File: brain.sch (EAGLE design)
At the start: 24 parts, among them IC1 LP2950ACZ-3.3, IC2 LP2950ACZ-3.3, U1 TINY45-20-DIP, U4 TINY45-20-DIP, U5 TINY45-20-DIP, U6 TINY45-20-DIP

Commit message: Added routing. Looks like everything should be good. Put in via line because the $33 boards don't support scoring.
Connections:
- removed net N$14: U5.PB3(ADC3)
- removed net N$7: U4.PB2(SCK/ADC1)
- new net PB22: U4.PB2(SCK/ADC1), U5.PB2(SCK/ADC1)
- net TX2: now also U5.PB3(ADC3); no longer U5.PB2(SCK/ADC1)
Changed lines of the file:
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@@
 </segment>
 <segment>
-<pinref part="U5" gate="G$1" pin="PB2(SCK/ADC1)"/>
-<wire x1="99.06" y1="-187.96" x2="101.6" y2="-187.96" width="0.1524" layer="91"/>
+<pinref part="U5" gate="G$1" pin="PB3(ADC3)"/>
+<wire x1="99.06" y1="-190.5" x2="101.6" y2="-190.5" width="0.1524" layer="91"/>
+<label x="101.6" y="-190.5" size="1.778" layer="95"/>
 </segment>
 </net>
@@
 <pinref part="U5" gate="G$1" pin="PB4(ADC2)"/>
 <wire x1="99.06" y1="-193.04" x2="101.6" y2="-193.04" width="0.1524" layer="91"/>
+<label x="101.6" y="-193.04" size="1.778" layer="95"/>
 </segment>
 </net>
 <net name="PB12" class="0">
+<segment>
+<pinref part="U5" gate="G$1" pin="PB1(MISO)"/>
+<wire x1="99.06" y1="-185.42" x2="101.6" y2="-185.42" width="0.1524" layer="91"/>
+<label x="101.6" y="-185.42" size="1.778" layer="95"/>
+</segment>
 <segment>
 <pinref part="U4" gate="G$1" pin="PB1(MISO)"/>
@@
 <pinref part="LED1" gate="G$1" pin="A"/>
 <wire x1="149.86" y1="-152.4" x2="157.48" y2="-152.4" width="0.1524" layer="91"/>
-</segment>
-<segment>
-<pinref part="U5" gate="G$1" pin="PB1(MISO)"/>
-<wire x1="99.06" y1="-185.42" x2="101.6" y2="-185.42" width="0.1524" layer="91"/>
+<label x="101.6" y="-154.94" size="1.778" layer="95"/>
 </segment>
 </net>
@@
 <pinref part="U4" gate="G$1" pin="PB0(MOSI)"/>
 <wire x1="99.06" y1="-152.4" x2="101.6" y2="-152.4" width="0.1524" layer="91"/>
+<label x="101.6" y="-152.4" size="1.778" layer="95"/>
 </segment>
 <segment>
 <pinref part="U5" gate="G$1" pin="PB0(MOSI)"/>
 <wire x1="99.06" y1="-182.88" x2="101.6" y2="-182.88" width="0.1524" layer="91"/>
-</segment>
-</net>
-<net name="N$7" class="0">
-<segment>
-<pinref part="U4" gate="G$1" pin="PB2(SCK/ADC1)"/>
-<wire x1="99.06" y1="-157.48" x2="101.6" y2="-157.48" width="0.1524" layer="91"/>
-</segment>
-</net>
-<net name="N$14" class="0">
-<segment>
-<pinref part="U5" gate="G$1" pin="PB3(ADC3)"/>
-<wire x1="99.06" y1="-190.5" x2="101.6" y2="-190.5" width="0.1524" layer="91"/>
+<label x="101.6" y="-182.88" size="1.778" layer="95"/>
 </segment>
 </net>
@@
 <pinref part="U5" gate="G$1" pin="PB5(NRES)"/>
 <wire x1="99.06" y1="-195.58" x2="101.6" y2="-195.58" width="0.1524" layer="91"/>
+<label x="101.6" y="-195.58" size="1.778" layer="95"/>
 </segment>
 <segment>
 <pinref part="U4" gate="G$1" pin="PB5(NRES)"/>
 <wire x1="99.06" y1="-165.1" x2="101.6" y2="-165.1" width="0.1524" layer="91"/>
+<label x="101.6" y="-165.1" size="1.778" layer="95"/>
 </segment>
 </net>
@@
 </segment>
 </net>
+<net name="PB22" class="0">
+<segment>
+<pinref part="U5" gate="G$1" pin="PB2(SCK/ADC1)"/>
+<wire x1="99.06" y1="-187.96" x2="101.6" y2="-187.96" width="0.1524" layer="91"/>
+<label x="101.6" y="-187.96" size="1.778" layer="95"/>
+</segment>
+<segment>
+<pinref part="U4" gate="G$1" pin="PB2(SCK/ADC1)"/>
+<wire x1="99.06" y1="-157.48" x2="101.6" y2="-157.48" width="0.1524" layer="91"/>
+<label x="101.6" y="-157.48" size="1.778" layer="95"/>
+</segment>
+</net>

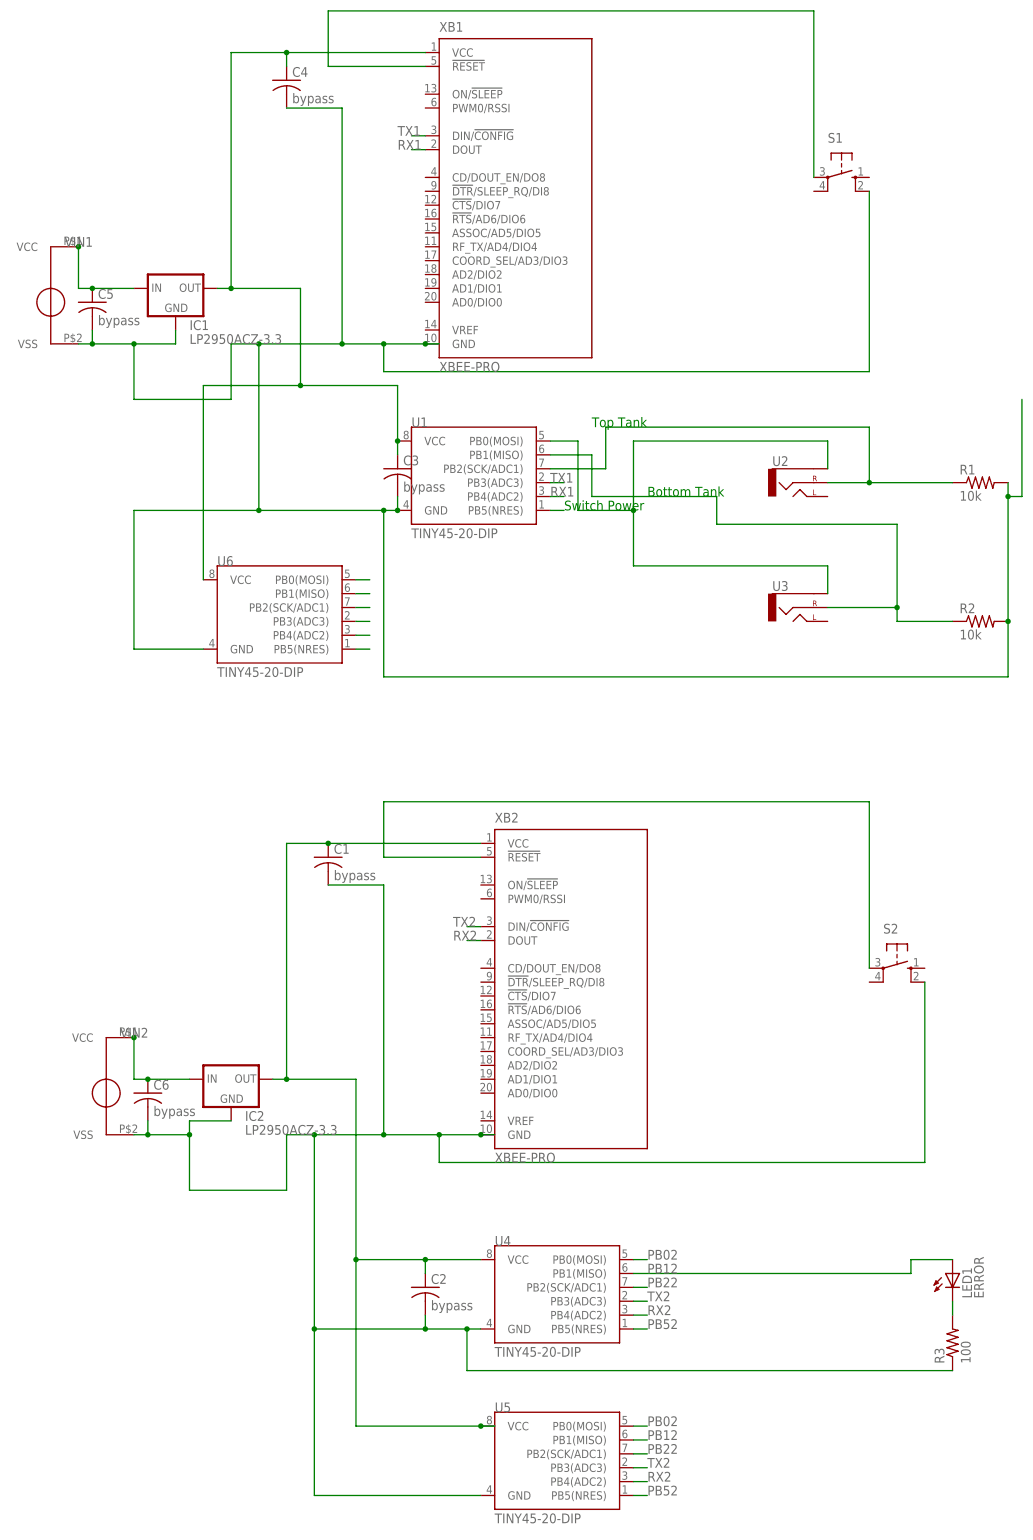
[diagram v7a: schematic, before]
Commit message: Added bypass capacitors per Sasha's request. Put some identifying information on bottom silkscreen.
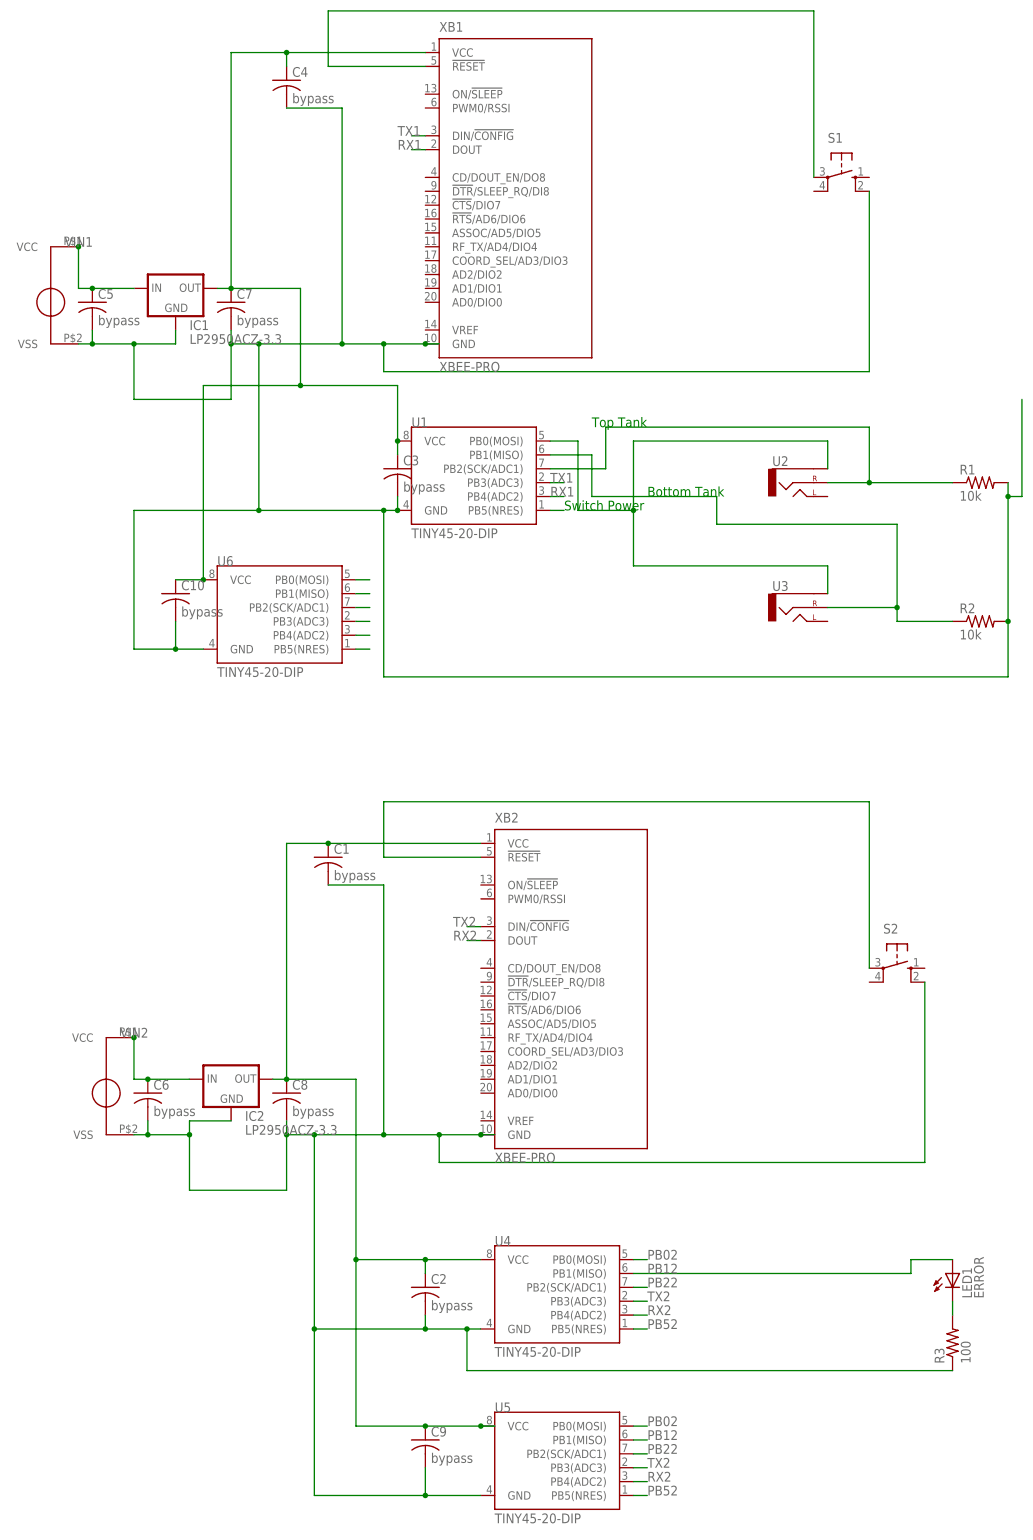
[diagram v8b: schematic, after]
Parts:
- added C10, C7, C8, C9: bypass, rcl:C-US050-025X075
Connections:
- net GND1: now also C10.2, C7.2
- net GND2: now also C8.2, C9.2
- net VCC1: now also C10.1, C7.1
- net VOUT2: now also C8.1, C9.1
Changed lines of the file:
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@@
 <part name="U5" library="SparkFun-DigitalIC" deviceset="ATTINY45" device="TINY45-20-DIP" value="TINY45-20-DIP"/>
 <part name="U6" library="SparkFun-DigitalIC" deviceset="ATTINY45" device="TINY45-20-DIP" value="TINY45-20-DIP"/>
+<part name="C7" library="rcl" deviceset="C-US" device="050-025X075" value="bypass"/>
+<part name="C8" library="rcl" deviceset="C-US" device="050-025X075" value="bypass"/>
+<part name="C9" library="rcl" deviceset="C-US" device="050-025X075" value="bypass"/>
+<part name="C10" library="rcl" deviceset="C-US" device="050-025X075" value="bypass"/>
 </parts>
 <sheets>
@@
 <instance part="U5" gate="G$1" x="86.36" y="-190.5"/>
 <instance part="U6" gate="G$1" x="35.56" y="-35.56"/>
+<instance part="C7" gate="G$1" x="25.4" y="22.86"/>
+<instance part="C8" gate="G$1" x="35.56" y="-121.92"/>
+<instance part="C9" gate="G$1" x="60.96" y="-185.42"/>
+<instance part="C10" gate="G$1" x="15.24" y="-30.48"/>
 </instances>
 <busses>
@@
 <wire x1="48.26" y1="-152.4" x2="48.26" y2="-182.88" width="0.1524" layer="91"/>
 <junction x="48.26" y="-152.4"/>
-<wire x1="48.26" y1="-182.88" x2="71.12" y2="-182.88" width="0.1524" layer="91"/>
+<wire x1="48.26" y1="-182.88" x2="60.96" y2="-182.88" width="0.1524" layer="91"/>
 <pinref part="U5" gate="G$1" pin="VCC"/>
+<wire x1="60.96" y1="-182.88" x2="71.12" y2="-182.88" width="0.1524" layer="91"/>
 <wire x1="73.66" y1="-182.88" x2="71.12" y2="-182.88" width="0.1524" layer="91"/>
 <junction x="71.12" y="-182.88"/>
+<pinref part="C8" gate="G$1" pin="1"/>
+<pinref part="C9" gate="G$1" pin="1"/>
+<junction x="60.96" y="-182.88"/>
 </segment>
 </net>
@@
 <junction x="40.64" y="-165.1"/>
 <pinref part="U5" gate="G$1" pin="GND"/>
-<wire x1="40.64" y1="-195.58" x2="71.12" y2="-195.58" width="0.1524" layer="91"/>
+<wire x1="40.64" y1="-195.58" x2="60.96" y2="-195.58" width="0.1524" layer="91"/>
+<pinref part="C8" gate="G$1" pin="2"/>
+<wire x1="60.96" y1="-195.58" x2="71.12" y2="-195.58" width="0.1524" layer="91"/>
+<wire x1="35.56" y1="-127" x2="35.56" y2="-129.54" width="0.1524" layer="91"/>
+<junction x="35.56" y="-129.54"/>
+<pinref part="C9" gate="G$1" pin="2"/>
+<wire x1="60.96" y1="-190.5" x2="60.96" y2="-195.58" width="0.1524" layer="91"/>
+<junction x="60.96" y="-195.58"/>
 </segment>
 </net>
@@
 <wire x1="7.62" y1="-15.24" x2="7.62" y2="-40.64" width="0.1524" layer="91"/>
 <pinref part="U6" gate="G$1" pin="GND"/>
-<wire x1="7.62" y1="-40.64" x2="20.32" y2="-40.64" width="0.1524" layer="91"/>
+<wire x1="7.62" y1="-40.64" x2="15.24" y2="-40.64" width="0.1524" layer="91"/>
+<pinref part="C7" gate="G$1" pin="2"/>
+<wire x1="15.24" y1="-40.64" x2="20.32" y2="-40.64" width="0.1524" layer="91"/>
+<wire x1="25.4" y1="17.78" x2="25.4" y2="15.24" width="0.1524" layer="91"/>
+<junction x="25.4" y="15.24"/>
+<pinref part="C10" gate="G$1" pin="2"/>
+<wire x1="15.24" y1="-35.56" x2="15.24" y2="-40.64" width="0.1524" layer="91"/>
+<junction x="15.24" y="-40.64"/>
 </segment>
 </net>
@@
 <wire x1="20.32" y1="7.62" x2="20.32" y2="-27.94" width="0.1524" layer="91"/>
 <junction x="38.1" y="7.62"/>
-</segment>
-</net>
+<pinref part="C7" gate="G$1" pin="1"/>
+<pinref part="C10" gate="G$1" pin="1"/>
+<wire x1="20.32" y1="-27.94" x2="15.24" y2="-27.94" width="0.1524" layer="91"/>
+<junction x="20.32" y="-27.94"/>
+</segment>
+</net>
